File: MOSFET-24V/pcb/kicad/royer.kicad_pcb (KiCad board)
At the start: 2 copper layers, 53.3 x 68.6 mm, 27 parts, among them J1 9-24V, J2 COIL, Q1 IRFB4410, Q2 IRFD110, Q3 IRFD110, Q4 IRFB4410

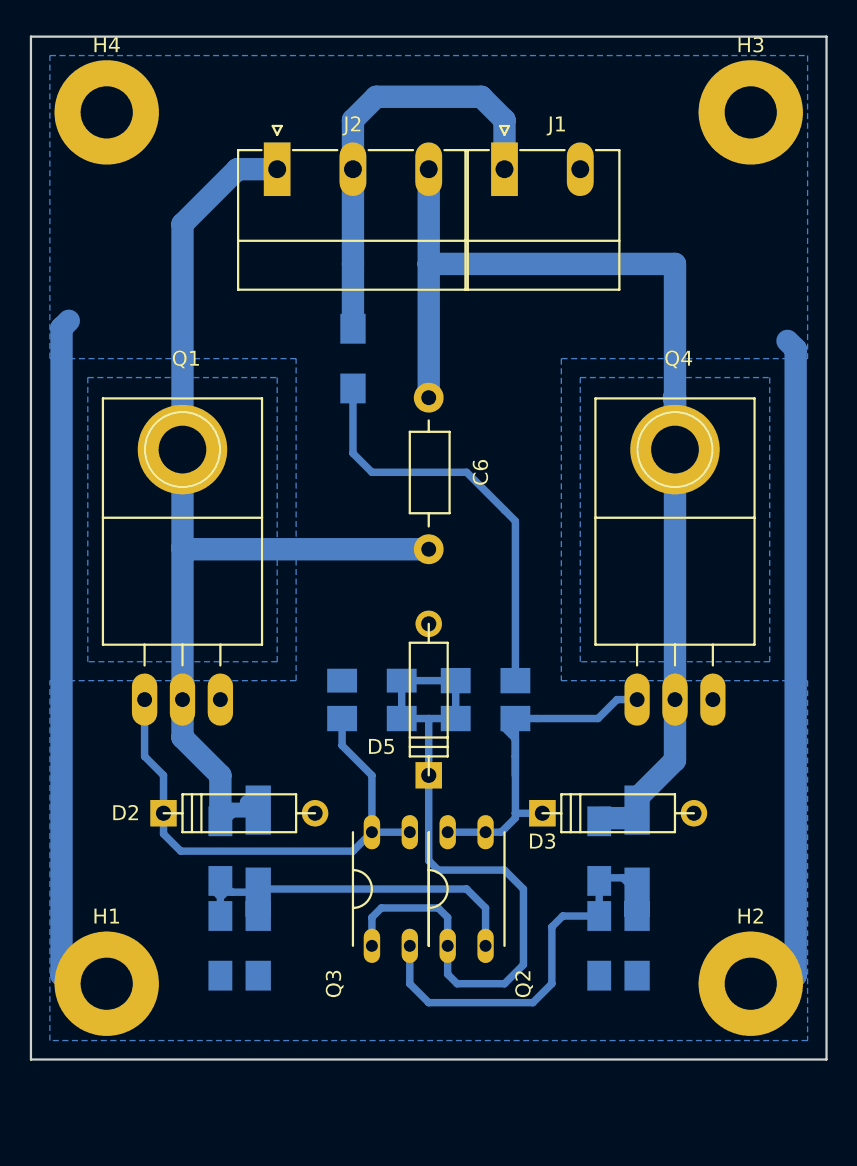
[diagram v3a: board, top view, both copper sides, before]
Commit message: footprint for small TO-220 heatsink
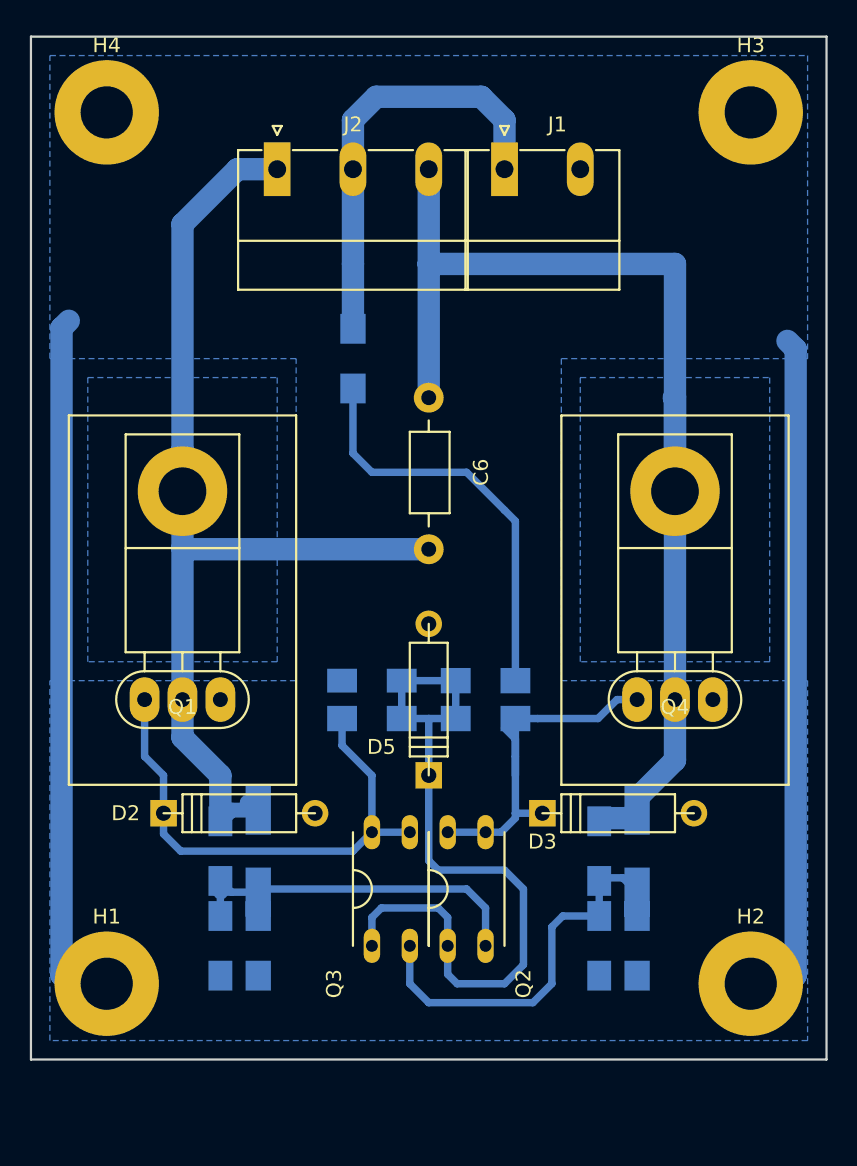
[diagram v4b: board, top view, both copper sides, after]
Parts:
- Q1, Q4: footprint TO-220:TO-220_Neutral123_Horizontal_LargePads -> TO-220-small-heatsink:TO-220-small-heatsink
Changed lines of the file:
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@@
     (links 49)
     (no_connects 0)
-    (area 151.054999 69.774999 204.545001 138.505001)
+    (area 135.660001 59.53 218.035 145.575001)
     (thickness 1.6)
     (drawings 8)
@@
     )
   )
-  (module TO-220:TO-220_Neutral123_Horizontal_LargePads (layer F.Cu)
-    (at 161.29 114.3)
-    (descr "TO-220, Neutral, Horizontal, Large Pads,")
-    (tags "TO-220, Neutral, Horizontal, Large Pads,")
-    (fp_text reference Q1 (at 0.24892 -22.84984) (layer F.SilkS)
-      (effects (font (size 1 1) (thickness 0.15)))
-    )
-    (fp_text value IRFB4410 (at -0.20066 4.24942) (layer F.Fab)
-      (effects (font (size 1 1) (thickness 0.15)))
-    )
-    (fp_line (start -2.54 -3.683) (end -2.54 -2.286) (layer F.SilkS) (width 0.15))
-    (fp_line (start 0 -3.683) (end 0 -2.286) (layer F.SilkS) (width 0.15))
-    (fp_line (start 2.54 -3.683) (end 2.54 -2.286) (layer F.SilkS) (width 0.15))
-    (fp_circle (center 0 -16.764) (end 1.778 -14.986) (layer F.SilkS) (width 0.15))
-    (fp_line (start 5.334 -12.192) (end 5.334 -20.193) (layer F.SilkS) (width 0.15))
-    (fp_line (start 5.334 -20.193) (end -5.334 -20.193) (layer F.SilkS) (width 0.15))
-    (fp_line (start -5.334 -20.193) (end -5.334 -12.192) (layer F.SilkS) (width 0.15))
-    (fp_line (start 5.334 -3.683) (end 5.334 -12.192) (layer F.SilkS) (width 0.15))
-    (fp_line (start 5.334 -12.192) (end -5.334 -12.192) (layer F.SilkS) (width 0.15))
-    (fp_line (start -5.334 -12.192) (end -5.334 -3.683) (layer F.SilkS) (width 0.15))
-    (fp_line (start 0 -3.683) (end -5.334 -3.683) (layer F.SilkS) (width 0.15))
-    (fp_line (start 0 -3.683) (end 5.334 -3.683) (layer F.SilkS) (width 0.15))
-    (pad 2 thru_hole oval (at 0 0 90) (size 3.50012 1.69926) (drill 1.00076) (layers *.Cu *.Mask)
-      (net 3 /C1))
-    (pad 1 thru_hole oval (at -2.54 0 90) (size 3.50012 1.69926) (drill 1.00076) (layers *.Cu *.Mask)
-      (net 8 /G1))
-    (pad 3 thru_hole oval (at 2.54 0 90) (size 3.50012 1.69926) (drill 1.00076) (layers *.Cu *.Mask)
-      (net 1 GND))
-    (pad 2 thru_hole circle (at 0 -16.764) (size 6 6) (drill 3.2) (layers *.Cu *.Mask)
-      (net 3 /C1))
-    (model TO_SOT_Packages_THT.3dshapes/TO-220_Neutral123_Horizontal_LargePads.wrl
-      (at (xyz 0 0 0))
-      (scale (xyz 0.3937 0.3937 0.3937))
-      (rotate (xyz 0 0 0))
-    )
-  )
-  (module TO-220:TO-220_Neutral123_Horizontal_LargePads (layer F.Cu)
-    (at 194.31 114.3)
-    (descr "TO-220, Neutral, Horizontal, Large Pads,")
-    (tags "TO-220, Neutral, Horizontal, Large Pads,")
-    (fp_text reference Q4 (at 0.24892 -22.84984) (layer F.SilkS)
-      (effects (font (size 1 1) (thickness 0.15)))
-    )
-    (fp_text value IRFB4410 (at -0.20066 4.24942) (layer F.Fab)
-      (effects (font (size 1 1) (thickness 0.15)))
-    )
-    (fp_line (start -2.54 -3.683) (end -2.54 -2.286) (layer F.SilkS) (width 0.15))
-    (fp_line (start 0 -3.683) (end 0 -2.286) (layer F.SilkS) (width 0.15))
-    (fp_line (start 2.54 -3.683) (end 2.54 -2.286) (layer F.SilkS) (width 0.15))
-    (fp_circle (center 0 -16.764) (end 1.778 -14.986) (layer F.SilkS) (width 0.15))
-    (fp_line (start 5.334 -12.192) (end 5.334 -20.193) (layer F.SilkS) (width 0.15))
-    (fp_line (start 5.334 -20.193) (end -5.334 -20.193) (layer F.SilkS) (width 0.15))
-    (fp_line (start -5.334 -20.193) (end -5.334 -12.192) (layer F.SilkS) (width 0.15))
-    (fp_line (start 5.334 -3.683) (end 5.334 -12.192) (layer F.SilkS) (width 0.15))
-    (fp_line (start 5.334 -12.192) (end -5.334 -12.192) (layer F.SilkS) (width 0.15))
-    (fp_line (start -5.334 -12.192) (end -5.334 -3.683) (layer F.SilkS) (width 0.15))
-    (fp_line (start 0 -3.683) (end -5.334 -3.683) (layer F.SilkS) (width 0.15))
-    (fp_line (start 0 -3.683) (end 5.334 -3.683) (layer F.SilkS) (width 0.15))
-    (pad 2 thru_hole oval (at 0 0 90) (size 3.50012 1.69926) (drill 1.00076) (layers *.Cu *.Mask)
-      (net 5 /C2))
-    (pad 1 thru_hole oval (at -2.54 0 90) (size 3.50012 1.69926) (drill 1.00076) (layers *.Cu *.Mask)
-      (net 9 /G2))
-    (pad 3 thru_hole oval (at 2.54 0 90) (size 3.50012 1.69926) (drill 1.00076) (layers *.Cu *.Mask)
-      (net 1 GND))
-    (pad 2 thru_hole circle (at 0 -16.764) (size 6 6) (drill 3.2) (layers *.Cu *.Mask)
-      (net 5 /C2))
-    (model TO_SOT_Packages_THT.3dshapes/TO-220_Neutral123_Horizontal_LargePads.wrl
-      (at (xyz 0 0 0))
-      (scale (xyz 0.3937 0.3937 0.3937))
-      (rotate (xyz 0 0 0))
-    )
-  )
   (module Choke_Axial_ThroughHole:Choke_Horizontal_RM10mm (layer F.Cu)
     (at 177.8 99.06 270)
@@
       (net 1 GND))
   )
+  (module TO-220-small-heatsink:TO-220-small-heatsink (layer F.Cu)
+    (at 161.29 114.3)
+    (fp_text reference Q1 (at 0 0.5) (layer F.SilkS)
+      (effects (font (size 1 1) (thickness 0.15)))
+    )
+    (fp_text value IRFB4410 (at 0 -0.5) (layer F.Fab)
+      (effects (font (size 1 1) (thickness 0.15)))
+    )
+    (fp_line (start -7.62 -19.05) (end -7.62 5.715) (layer F.SilkS) (width 0.15))
+    (fp_line (start 7.62 -19.05) (end -7.62 -19.05) (layer F.SilkS) (width 0.15))
+    (fp_line (start 7.62 5.715) (end 7.62 -19.05) (layer F.SilkS) (width 0.15))
+    (fp_line (start -7.62 5.715) (end 7.62 5.715) (layer F.SilkS) (width 0.15))
+    (fp_line (start -2.54 1.905) (end 2.54 1.905) (layer F.SilkS) (width 0.15))
+    (fp_line (start -2.54 -1.905) (end 2.54 -1.905) (layer F.SilkS) (width 0.15))
+    (fp_arc (start -2.54 0) (end -2.54 1.905) (angle 180) (layer F.SilkS) (width 0.15))
+    (fp_line (start 2.54 -3.175) (end 2.54 -1.905) (layer F.SilkS) (width 0.15))
+    (fp_line (start 0 -3.175) (end 0 -1.905) (layer F.SilkS) (width 0.15))
+    (fp_line (start -2.54 -3.175) (end -2.54 -1.905) (layer F.SilkS) (width 0.15))
+    (fp_line (start -3.81 -10.16) (end 3.81 -10.16) (layer F.SilkS) (width 0.15))
+    (fp_line (start -3.81 -17.78) (end 3.81 -17.78) (layer F.SilkS) (width 0.15))
+    (fp_line (start 3.81 -17.78) (end 3.81 -3.175) (layer F.SilkS) (width 0.15))
+    (fp_line (start 3.81 -3.175) (end -3.81 -3.175) (layer F.SilkS) (width 0.15))
+    (fp_line (start -3.81 -3.175) (end -3.81 -17.78) (layer F.SilkS) (width 0.15))
+    (fp_arc (start 2.54 0) (end 2.54 -1.905) (angle 180) (layer F.SilkS) (width 0.15))
+    (pad 1 thru_hole oval (at -2.54 0) (size 2 3) (drill 1) (layers *.Cu *.Mask)
+      (net 8 /G1))
+    (pad 2 thru_hole oval (at 0 0) (size 2 3) (drill 1) (layers *.Cu *.Mask)
+      (net 3 /C1))
+    (pad 3 thru_hole oval (at 2.54 0) (size 2 3) (drill 1) (layers *.Cu *.Mask)
+      (net 1 GND))
+    (pad 2 thru_hole circle (at 0 -13.97) (size 6 6) (drill 3.2) (layers *.Cu *.Mask)
+      (net 3 /C1))
+  )
+  (module TO-220-small-heatsink:TO-220-small-heatsink (layer F.Cu)
+    (at 194.31 114.3)
+    (fp_text reference Q4 (at 0 0.5) (layer F.SilkS)
+      (effects (font (size 1 1) (thickness 0.15)))
+    )
+    (fp_text value IRFB4410 (at 0 -0.5) (layer F.Fab)
+      (effects (font (size 1 1) (thickness 0.15)))
+    )
+    (fp_line (start -7.62 -19.05) (end -7.62 5.715) (layer F.SilkS) (width 0.15))
+    (fp_line (start 7.62 -19.05) (end -7.62 -19.05) (layer F.SilkS) (width 0.15))
+    (fp_line (start 7.62 5.715) (end 7.62 -19.05) (layer F.SilkS) (width 0.15))
+    (fp_line (start -7.62 5.715) (end 7.62 5.715) (layer F.SilkS) (width 0.15))
+    (fp_line (start -2.54 1.905) (end 2.54 1.905) (layer F.SilkS) (width 0.15))
+    (fp_line (start -2.54 -1.905) (end 2.54 -1.905) (layer F.SilkS) (width 0.15))
+    (fp_arc (start -2.54 0) (end -2.54 1.905) (angle 180) (layer F.SilkS) (width 0.15))
+    (fp_line (start 2.54 -3.175) (end 2.54 -1.905) (layer F.SilkS) (width 0.15))
+    (fp_line (start 0 -3.175) (end 0 -1.905) (layer F.SilkS) (width 0.15))
+    (fp_line (start -2.54 -3.175) (end -2.54 -1.905) (layer F.SilkS) (width 0.15))
+    (fp_line (start -3.81 -10.16) (end 3.81 -10.16) (layer F.SilkS) (width 0.15))
+    (fp_line (start -3.81 -17.78) (end 3.81 -17.78) (layer F.SilkS) (width 0.15))
+    (fp_line (start 3.81 -17.78) (end 3.81 -3.175) (layer F.SilkS) (width 0.15))
+    (fp_line (start 3.81 -3.175) (end -3.81 -3.175) (layer F.SilkS) (width 0.15))
+    (fp_line (start -3.81 -3.175) (end -3.81 -17.78) (layer F.SilkS) (width 0.15))
+    (fp_arc (start 2.54 0) (end 2.54 -1.905) (angle 180) (layer F.SilkS) (width 0.15))
+    (pad 1 thru_hole oval (at -2.54 0) (size 2 3) (drill 1) (layers *.Cu *.Mask)
+      (net 9 /G2))
+    (pad 2 thru_hole oval (at 0 0) (size 2 3) (drill 1) (layers *.Cu *.Mask)
+      (net 5 /C2))
+    (pad 3 thru_hole oval (at 2.54 0) (size 2 3) (drill 1) (layers *.Cu *.Mask)
+      (net 1 GND))
+    (pad 2 thru_hole circle (at 0 -13.97) (size 6 6) (drill 3.2) (layers *.Cu *.Mask)
+      (net 5 /C2))
+  )
   (dimension 58.42 (width 0.3) (layer Eco2.User)

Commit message: compacting PCB
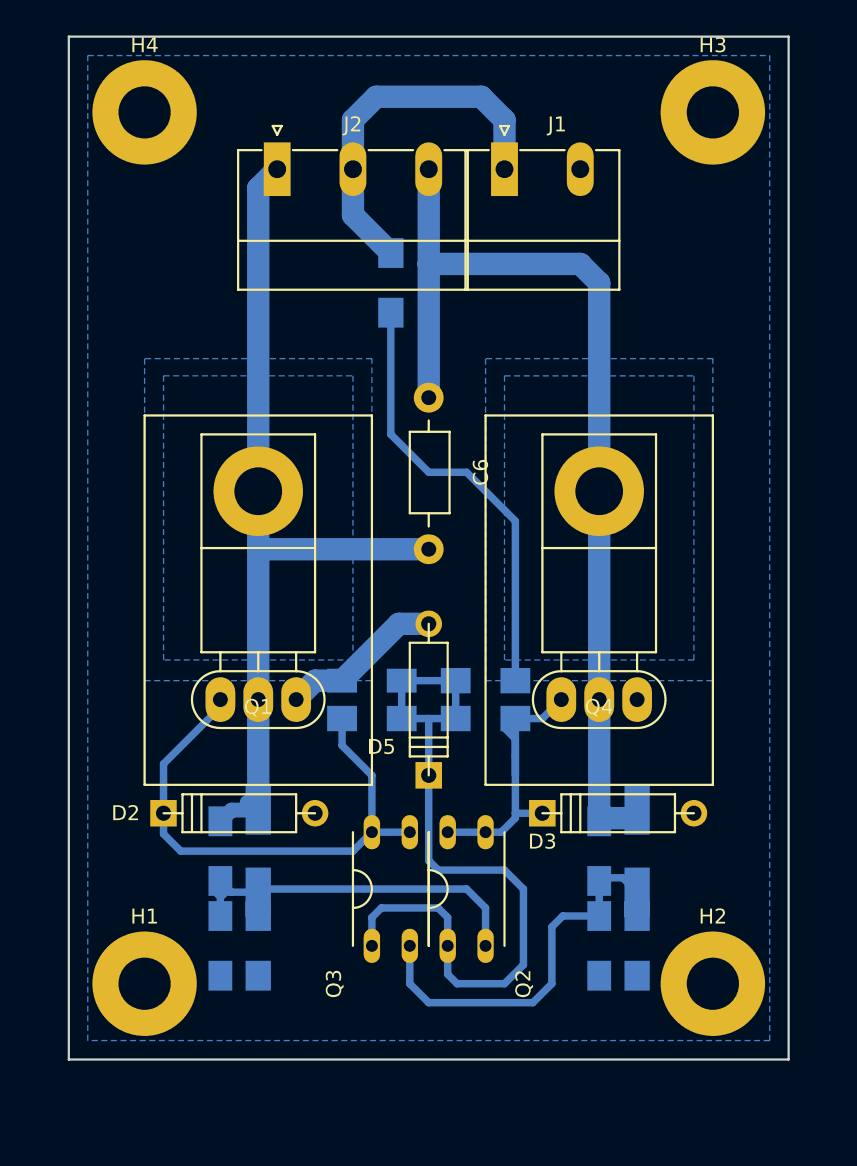
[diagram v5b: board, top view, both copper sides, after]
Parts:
- moved R6 5.68 mm to (175.3, 86.4)
- moved Q1 5.08 mm to (166.4, 114.3)
- moved Q4 5.08 mm to (189.2, 114.3)
- moved H1 2.54 mm to (158.8, 133.3)
- moved H2 2.54 mm to (196.8, 133.3)
- moved H3 2.54 mm to (196.8, 74.9)
- moved H4 2.54 mm to (158.8, 74.9)
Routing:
- net GND: track 93.6 -> 11.0 mm
- net /C1: track 69.3 -> 58.8 mm
- net /C2: track 76.2 -> 67.2 mm
- net /G2: track 25.6 -> 20.5 mm
- net /24V: track 28.8 -> 24.7 mm
- net Net-(R5-Pad1): track 27.8 -> 29.6 mm
- net /G1: track 35.5 -> 36.5 mm
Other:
- board size 53.3 x 68.6 mm -> 48.3 x 68.6 mm

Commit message: compacting PCB
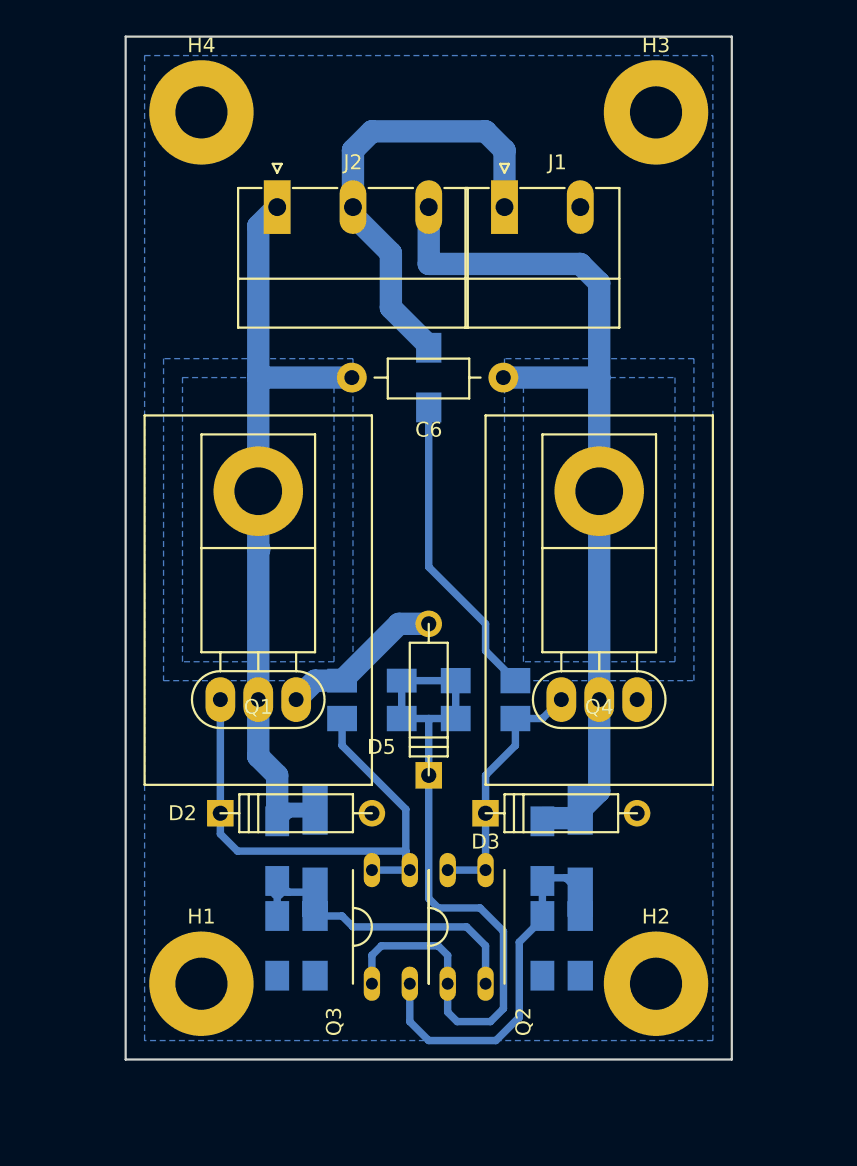
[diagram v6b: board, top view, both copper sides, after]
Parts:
- moved R6 6.84 mm to (177.8, 92.7)
- moved C6 6.35 mm to (177.8, 92.7), turned to 180 degrees
- moved C3 3.81 mm to (185.4, 130.8)
- moved C4 3.81 mm to (185.4, 124.5)
- moved D1 3.81 mm to (170.2, 124.5)
- moved D2 3.81 mm to (168.9, 121.9)
- moved D3 3.81 mm to (186.7, 121.9)
- moved D4 3.81 mm to (188.0, 124.5)
- moved H1 3.81 mm to (162.6, 133.3)
- moved H2 3.81 mm to (193.0, 133.3)
- moved H3 3.81 mm to (193.0, 74.9)
- moved H4 3.81 mm to (162.6, 74.9)
- moved R1 3.81 mm to (170.2, 130.8)
- moved R4 3.81 mm to (188.0, 130.8)
- moved C1 3.81 mm to (167.6, 124.5)
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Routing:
- net Net-(R5-Pad1): track 29.6 -> 20.7 mm
- net /C1: track 58.8 -> 51.7 mm
- net /C2: track 67.2 -> 61.9 mm
- net /24V: track 24.7 -> 29.8 mm
- net /G2: track 20.5 -> 17.1 mm
- net /D1: track 24.4 -> 21.1 mm
- net /D2: track 29.1 -> 27.2 mm
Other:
- board size 48.3 x 68.6 mm -> 40.6 x 68.6 mm

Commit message: compacting PCB (using only 4 screw terminals)
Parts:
- removed J2: COIL, Connectors_Phoenix:PhoenixContact_MC-G_03x5.08mm_Angled
- J1: value 9-24V -> Screw_Terminal_1x04; footprint Connectors_Phoenix:PhoenixContact_MC-G_02x5.08mm_Angled -> Connectors_Phoenix:PhoenixContact_MCV-G_04x5.08mm_Vertical
- moved J1 13.0 mm to (170.2, 83.8)
- moved H3 8.89 mm to (193.0, 83.8)
- moved H4 7.62 mm to (162.6, 82.5)
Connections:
- J1 pad 1: /24V -> /C1
- J1 pad 2: GND -> /24V
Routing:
- net /24V: track 29.8 -> 7.40 mm
- net /C2: track 61.9 -> 48.7 mm
- net /C1: track 51.7 -> 48.6 mm
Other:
- board size 40.6 x 68.6 mm -> 40.6 x 59.7 mm
